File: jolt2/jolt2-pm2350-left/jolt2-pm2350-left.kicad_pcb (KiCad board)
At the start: 2 copper layers, 151 x 98 mm, 34 parts, among them J1 Conn_01x02_Pin, J10 Conn_01x02_Pin, J11 Conn_01x02_Pin, J12 Conn_01x02_Pin, J13 Conn_01x02_Pin, J14 Conn_01x02_Pin, J15 Conn_01x02_Pin, J16 Conn_01x02_Pin, J17 Conn_01x02_Pin, J18 Conn_01x02_Pin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

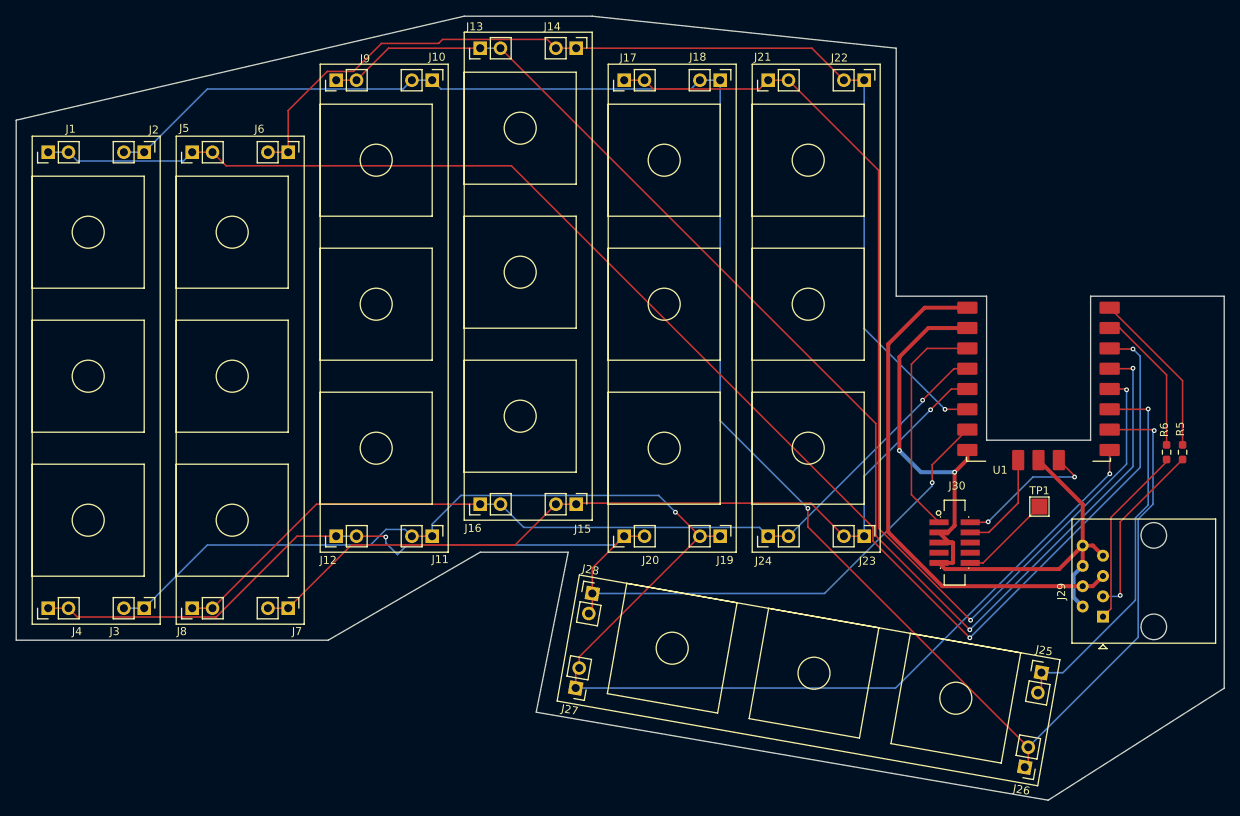
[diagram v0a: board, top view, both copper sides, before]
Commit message: jolt2: Update pm2350 left footprint
Build the footprint, updating it for the left side of the keyboard
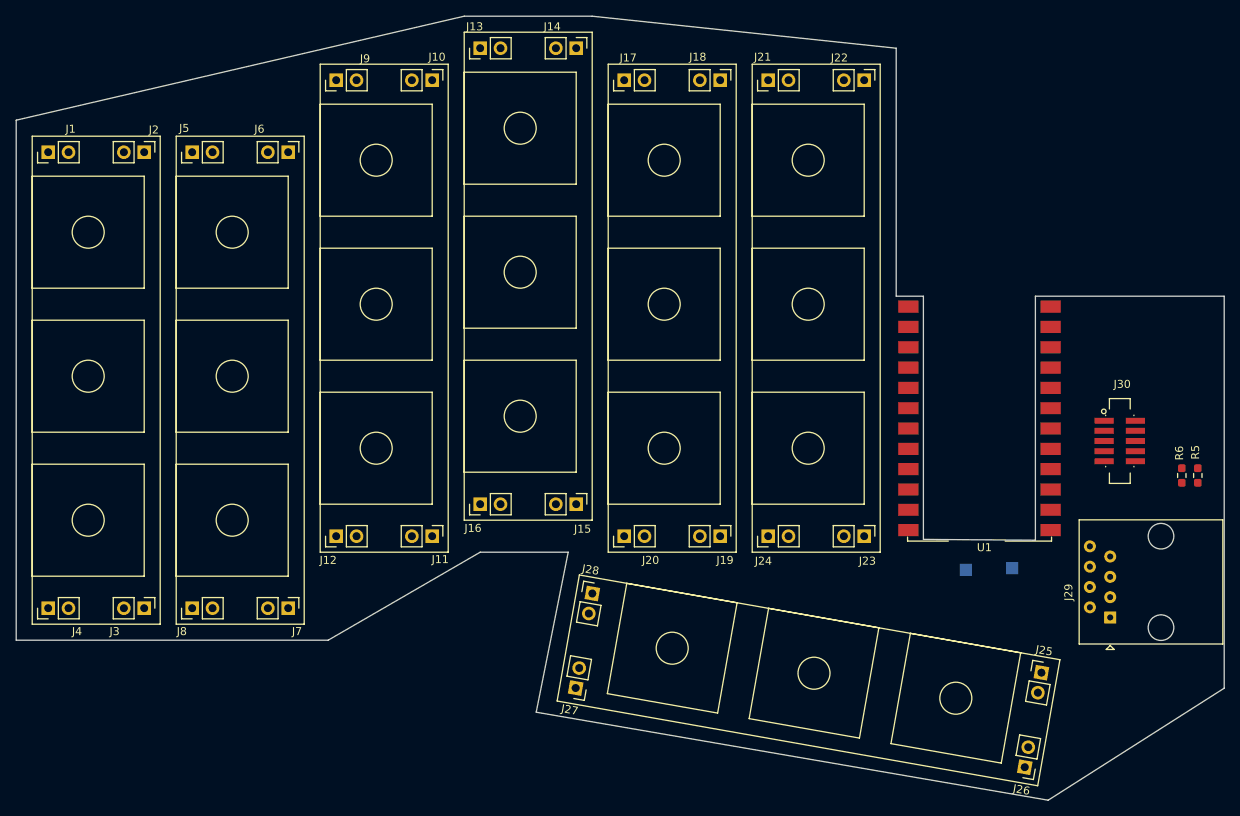
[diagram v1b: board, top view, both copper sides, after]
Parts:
- removed TP1: Reset, TestPoint:TestPoint_Pad_2.0x2.0mm
- added TP2: SWDIO, TestPoint:TestPoint_Pad_1.5x1.5mm, B.Cu at (155.7, 137.2)
- added TP3: SWCLK, TestPoint:TestPoint_Pad_1.5x1.5mm, B.Cu at (161.5, 137.0)
- U1: footprint davidb-keyboard-foot:Pimoroni-Tiny2040 -> davidb-keyboard-foot:SparkFun_Pro_Micro_RP2350
- moved U1 25.9 mm to (148.5, 133.5)
- moved J30 24.2 mm to (174.9, 121.1)
- moved R5 3.48 mm to (184.7, 125.4)
- moved R6 3.48 mm to (182.7, 125.4)
- moved J29 0.91 mm to (173.8, 143.2)
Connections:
- U1 pad 2: /COL-A -> /ROW-A
- U1 pad 3: /COL-B -> /ROW-B
- U1 pad 4: /COL-C -> /ROW-C
- U1 pad 5: /COL-D -> /ROW-D
- U1 pad 6: /ROW-A -> /ROW-E
- U1 pad 7: /ROW-B -> /ROW-F
- U1 pad A0: /ROW-C -> /COL-A
- U1 pad A1: /ROW-D -> /COL-B
- U1 pad A2: /ROW-E -> /COL-C
- U1 pad A3: /ROW-F -> /COL-D
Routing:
- net /ROW-A: track 232.9 -> 0.00 mm, vias 2 -> 0
- net /COL-A: track 190.5 -> 0.00 mm, vias 2 -> 0
- net /ROW-B: track 190.3 -> 0.00 mm, vias 2 -> 0
- net /COL-B: track 163.3 -> 0.00 mm, vias 2 -> 0
- net /ROW-C: track 149.9 -> 0.00 mm, vias 2 -> 0
- net /COL-C: track 137.4 -> 0.00 mm, vias 2 -> 0
- net /ROW-D: track 133.7 -> 0.00 mm, vias 1 -> 0
- net /ROW-F: track 112.8 -> 0.00 mm, vias 1 -> 0
- net /ROW-E: track 106.6 -> 0.00 mm, vias 1 -> 0
- net GND: track 94.5 -> 0.00 mm, vias 2 -> 0
- net VBUS: track 65.5 -> 0.00 mm
- net /COL-D: track 47.6 -> 0.00 mm, vias 1 -> 0
- net +3.3V: track 29.0 -> 0.00 mm
- net SERRX: track 22.9 -> 0.00 mm
- net SERTX: track 22.4 -> 0.00 mm, vias 1 -> 0
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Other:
- outline, holes or cut-outs redrawn
